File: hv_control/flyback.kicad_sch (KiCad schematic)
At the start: 33 parts, among them Q1 TCLT1003, U30 FSL4110LR, U31 ${SIM.PARAMS}

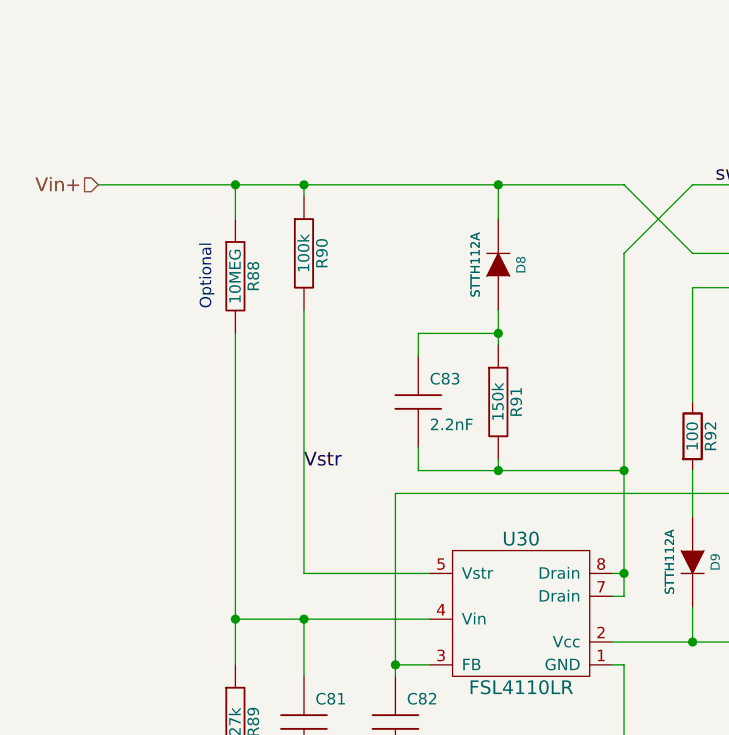
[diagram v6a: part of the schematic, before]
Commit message: Update flyback resistors, we're below 700V.
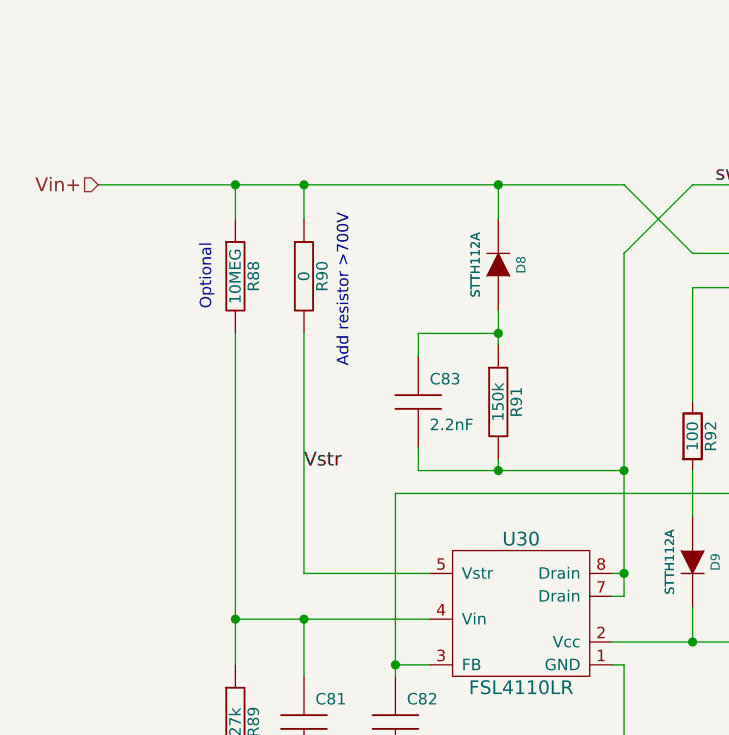
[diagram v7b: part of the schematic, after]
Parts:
- R90: value 100k -> 0
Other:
- note added: "Add resistor >700V"
- moved on the sheet: R90
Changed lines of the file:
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@@
     (stroke (width 0) (type solid))
   )
-  (wire (pts (xy 82.55 63.5) (xy 82.55 92.71))
+  (wire (pts (xy 82.55 66.04) (xy 82.55 92.71))
     (stroke (width 0) (type solid))
   )
@@
     (stroke (width 0) (type solid))
   )
-  (wire (pts (xy 82.55 49.53) (xy 82.55 50.8))
+  (wire (pts (xy 82.55 49.53) (xy 82.55 53.34))
     (stroke (width 0) (type solid))
   )
@@
     (effects (font (size 1.524 1.524)) (justify left bottom))
   )
+  (text "Add resistor >700V" (at 87.63 69.85 90)
+    (effects (font (size 1.27 1.27)) (justify left bottom))
+  )
   (text "4.7k -> 6.2k for Cree FETS" (at 181.61 148.59 0)
     (effects (font (size 1.524 1.524)) (justify left bottom))
@@
     )
   )
-  (symbol (lib_id "Local:R") (at 82.55 57.15 0) (unit 1)
-    (in_bom yes) (on_board yes) (dnp no)
-    (property "Reference" "R90" (at 84.582 57.15 90)
-      (effects (font (size 1.27 1.27)))
-    )
-    (property "Value" "100k" (at 82.55 57.15 90)
-      (effects (font (size 1.27 1.27)))
-    )
-    (property "Footprint" "Resistor_SMD:R_1206_3216Metric" (at 82.55 57.15 0)
-      (effects (font (size 1.524 1.524)) hide)
-    )
-    (property "Datasheet" "" (at 82.55 57.15 0)
-      (effects (font (size 1.524 1.524)))
-    )
-    (property "Manufacturer" "BOURNS" (at 82.55 57.15 0)
-      (effects (font (size 1.27 1.27)) hide)
-    )
-    (property "PartNr" "CHV1206-FX-1003ELF" (at 82.55 57.15 0)
-      (effects (font (size 1.27 1.27)) hide)
-    )
-    (property "Farnell" "2470926" (at 82.55 57.15 0)
-      (effects (font (size 1.524 1.524)) hide)
-    )
-    (property "Digikey" "CHV1206-FX-1003ELFCT-ND" (at 82.55 57.15 0)
-      (effects (font (size 1.27 1.27)) hide)
-    )
-    (property "domain" "1-2=1.3" (at 82.55 57.15 90)
-      (effects (font (size 1.27 1.27)) hide)
-    )
+  (symbol (lib_id "Local:R") (at 82.55 59.69 0) (unit 1)
+    (in_bom yes) (on_board yes) (dnp no)
+    (property "Reference" "R90" (at 84.582 59.69 90)
+      (effects (font (size 1.27 1.27)))
+    )
+    (property "Value" "0" (at 82.55 59.69 90)
+      (effects (font (size 1.27 1.27)))
+    )
+    (property "Footprint" "Resistor_SMD:R_1206_3216Metric" (at 82.55 59.69 0)
+      (effects (font (size 1.524 1.524)) hide)
+    )
+    (property "Datasheet" "" (at 82.55 59.69 0)
+      (effects (font (size 1.524 1.524)))
+    )
+    (property "Manufacturer" "BOURNS" (at 82.55 59.69 0)
+      (effects (font (size 1.27 1.27)) hide)
+    )
+    (property "PartNr" "CHV1206-FX-1003ELF" (at 82.55 59.69 0)
+      (effects (font (size 1.27 1.27)) hide)
+    )
+    (property "Farnell" "2470926" (at 82.55 59.69 0)
+      (effects (font (size 1.524 1.524)) hide)
+    )
+    (property "Digikey" "CHV1206-FX-1003ELFCT-ND" (at 82.55 59.69 0)
+      (effects (font (size 1.27 1.27)) hide)
+    )
+    (property "domain" "1-2=1.3" (at 82.55 59.69 90)
+      (effects (font (size 1.27 1.27)) hide)
+    )
